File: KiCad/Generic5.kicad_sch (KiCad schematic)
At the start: 28 parts, among them J1 Conn_01x04, J2 USB-C, U1 ESP32-PICO-MINI-02, U2 FT231XQ, U3 LMR16006+FB

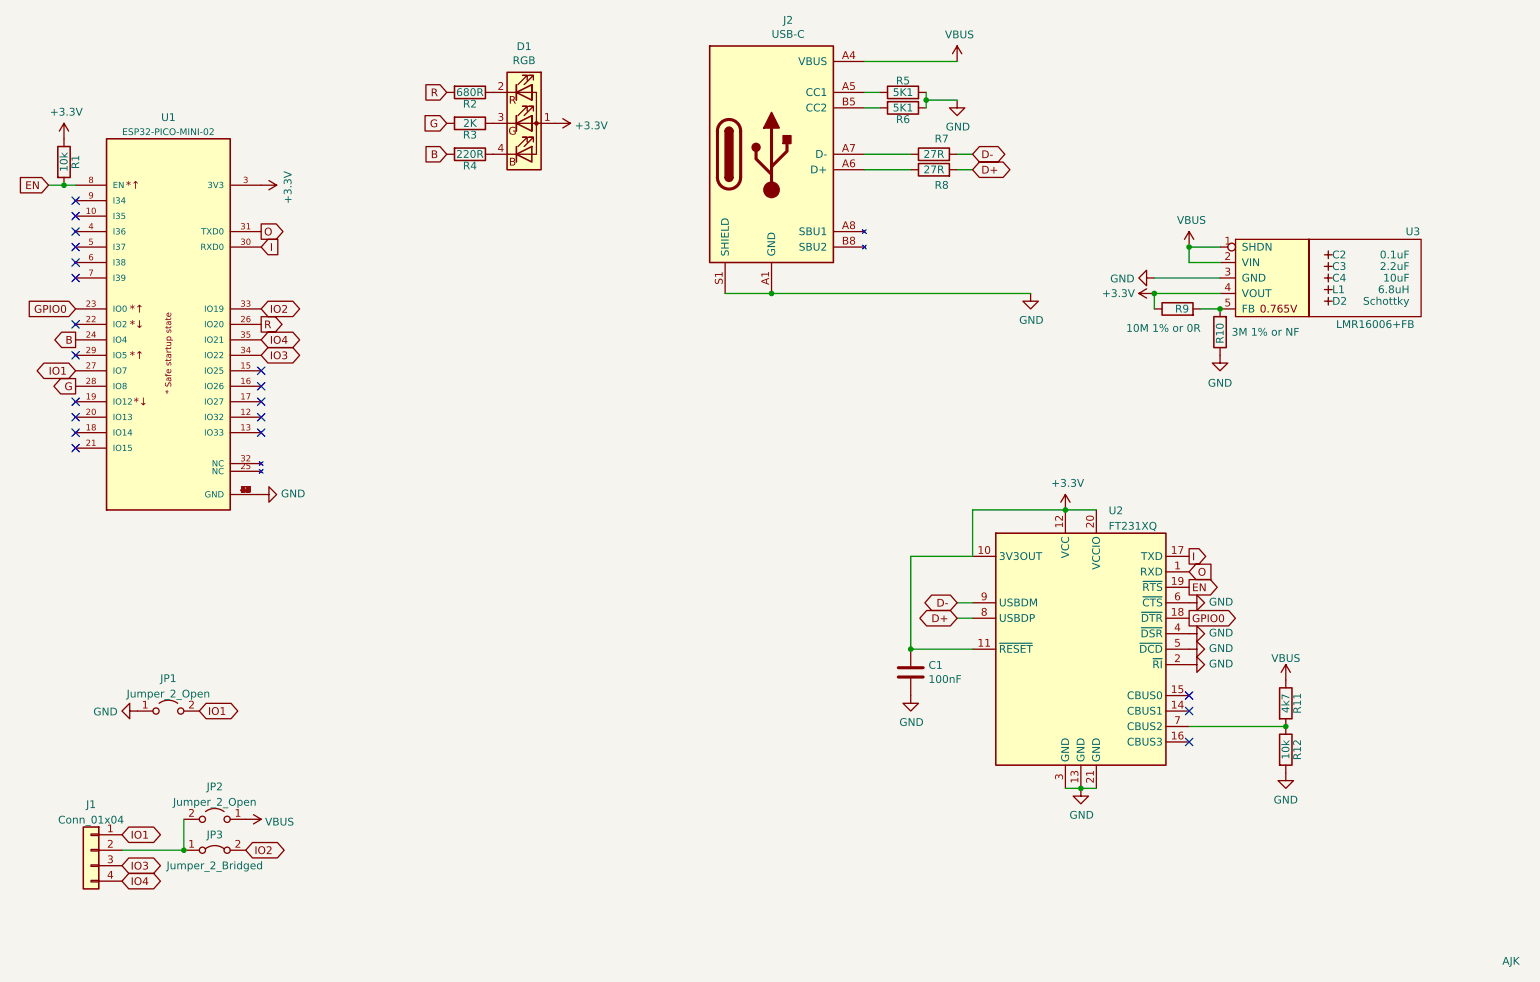
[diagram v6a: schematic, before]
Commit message: FET and diode logic
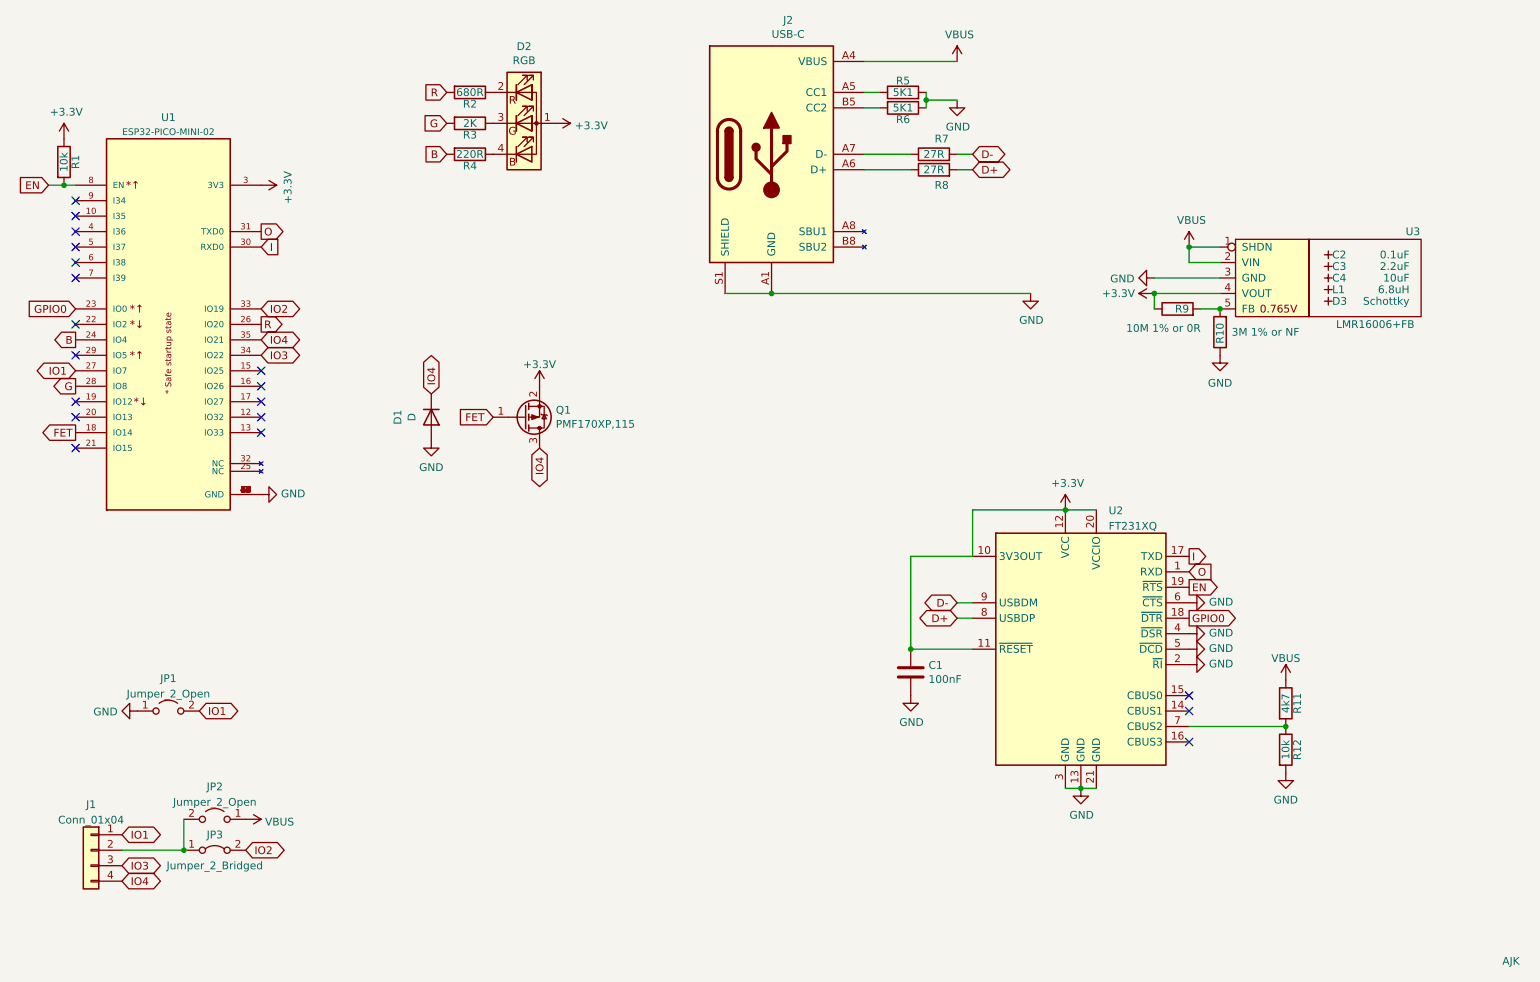
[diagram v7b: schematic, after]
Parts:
- added D1: D, Diode_SMD:D_1206_3216Metric, symbol Device:D
- added Q1: PMF170XP,115, Package_TO_SOT_SMD:SOT-323_SC-70, symbol Device:Q_PMOS_GSD
- renumbered D1 to D2, D2 to D3
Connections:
- net +3V3: now also Q1.2 (S)
- net GND: now also D1.2 (A)
- net IO4: now also D1.1 (K), Q1.3 (D)
- net FET: now reaches U1.18 (IO14)
- net FET: now also Q1.1 (G)
- no-connect marks 20 -> 19
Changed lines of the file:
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@@
   (no_connect (at 43.18 58.42))
   (no_connect (at 43.18 83.82))
-  (no_connect (at 43.18 86.36))
   (no_connect (at 73.66 83.82))
   (wire (pts (xy 226.06 134.62) (xy 241.935 134.62))
@@
     )
   )
+  (global_label "IO4" (shape bidirectional) (at 101.6 80.01 90) (fields_autoplaced)
+    (effects (font (size 1.27 1.27)) (justify left))
+    (property "Intersheet References" "${INTERSHEET_REFS}" (id 0) (at 16.51 160.655 0)
+      (effects (font (size 1.27 1.27)) hide)
+    )
+  )
   (global_label "IO2" (shape bidirectional) (at 71.12 154.94 0) (fields_autoplaced)
     (effects (font (size 1.27 1.27)) (justify left))
@@
     (property "Intersheet References" "${INTERSHEET_REFS}" (id 0) (at -6.985 -19.05 0)
       (effects (font (size 1.27 1.27)) hide)
+    )
+  )
+  (global_label "IO4" (shape bidirectional) (at 119.38 88.9 270) (fields_autoplaced)
+    (effects (font (size 1.27 1.27)) (justify right))
+    (property "Intersheet References" "${INTERSHEET_REFS}" (id 0) (at 204.47 8.255 0)
+      (effects (font (size 1.27 1.27)) hide)
+    )
+  )
+  (global_label "FET" (shape output) (at 43.18 86.36 180) (fields_autoplaced)
+    (effects (font (size 1.27 1.27)) (justify right))
+    (property "Intersheet References" "${INTERSHEET_REFS}" (id 0) (at 37.6506 86.2806 0)
+      (effects (font (size 1.27 1.27)) (justify right) hide)
     )
   )
@@
     )
   )
+  (global_label "FET" (shape input) (at 111.76 83.82 180) (fields_autoplaced)
+    (effects (font (size 1.27 1.27)) (justify right))
+    (property "Intersheet References" "${INTERSHEET_REFS}" (id 0) (at 106.2306 83.7406 0)
+      (effects (font (size 1.27 1.27)) (justify right) hide)
+    )
+  )
   (global_label "IO4" (shape bidirectional) (at 50.8 160.02 0) (fields_autoplaced)
     (effects (font (size 1.27 1.27)) (justify left))
@@
   (symbol (lib_id "Device:LED_ARGB") (at 116.84 35.56 0) (unit 1)
     (in_bom yes) (on_board yes)
-    (property "Reference" "D1" (id 0) (at 116.84 22.9362 0))
+    (property "Reference" "D2" (id 0) (at 116.84 22.9362 0))
     (property "Value" "RGB" (id 1) (at 116.84 25.2476 0))
     (property "Footprint" "RevK:LED-RGB-1.6x1.6" (id 2) (at 116.84 36.83 0)
@@
   (symbol (lib_id "RevK:Hidden") (at 248.92 64.77 0) (unit 1)
     (in_bom yes) (on_board yes)
-    (property "Reference" "D2" (id 0) (at 249.555 64.77 0)
+    (property "Reference" "D3" (id 0) (at 249.555 64.77 0)
       (effects (font (size 1.27 1.27)) (justify left))
     )
@@
     (pin "1")
   )
+  (symbol (lib_id "Device:Q_PMOS_GSD") (at 116.84 83.82 0) (mirror x) (unit 1)
+    (in_bom yes) (on_board yes)
+    (property "Reference" "Q1" (id 0) (at 122.047 82.6516 0)
+      (effects (font (size 1.27 1.27)) (justify left))
+    )
+    (property "Value" "PMF170XP,115" (id 1) (at 122.047 84.963 0)
+      (effects (font (size 1.27 1.27)) (justify left))
+    )
+    (property "Footprint" "Package_TO_SOT_SMD:SOT-323_SC-70" (id 2) (at 121.92 86.36 0)
+      (effects (font (size 1.27 1.27)) hide)
+    )
+    (property "Datasheet" "~" (id 3) (at 116.84 83.82 0)
+      (effects (font (size 1.27 1.27)) hide)
+    )
+    (property "Note" "Any P-Channel SOT323 that does 3.3V/0.5A" (id 4) (at 116.84 83.82 0)
+      (effects (font (size 1.27 1.27)) hide)
+    )
+    (pin "1")
+    (pin "2")
+    (pin "3")
+  )
   (symbol (lib_id "power:GND") (at 231.14 73.66 0) (unit 1)
     (in_bom yes) (on_board yes) (fields_autoplaced)
@@
     )
     (property "Datasheet" "" (id 3) (at 53.34 132.08 0)
+      (effects (font (size 1.27 1.27)) hide)
+    )
+    (pin "1")
+  )
+  (symbol (lib_id "power:+3.3V") (at 119.38 78.74 0) (unit 1)
+    (in_bom yes) (on_board yes) (fields_autoplaced)
+    (property "Reference" "#PWR0101" (id 0) (at 119.38 82.55 0)
+      (effects (font (size 1.27 1.27)) hide)
+    )
+    (property "Value" "+3.3V" (id 1) (at 119.38 75.1642 0))
+    (property "Footprint" "" (id 2) (at 119.38 78.74 0)
+      (effects (font (size 1.27 1.27)) hide)
+    )
+    (property "Datasheet" "" (id 3) (at 119.38 78.74 0)
       (effects (font (size 1.27 1.27)) hide)
     )
@@
     (pin "2")
   )
+  (symbol (lib_id "power:GND") (at 101.6 87.63 0) (unit 1)
+    (in_bom yes) (on_board yes) (fields_autoplaced)
+    (property "Reference" "#PWR?" (id 0) (at 101.6 93.98 0)
+      (effects (font (size 1.27 1.27)) hide)
+    )
+    (property "Value" "GND" (id 1) (at 101.6 92.0734 0))
+    (property "Footprint" "" (id 2) (at 101.6 87.63 0)
+      (effects (font (size 1.27 1.27)) hide)
+    )
+    (property "Datasheet" "" (id 3) (at 101.6 87.63 0)
+      (effects (font (size 1.27 1.27)) hide)
+    )
+    (pin "1")
+  )
   (symbol (lib_id "Connector_Generic:Conn_01x04") (at 45.72 154.94 0) (mirror y) (unit 1)
     (in_bom yes) (on_board yes) (fields_autoplaced)
@@
     (pin "5")
   )
+  (symbol (lib_id "Device:D") (at 101.6 83.82 270) (unit 1)
+    (in_bom yes) (on_board yes)
+    (property "Reference" "D1" (id 0) (at 96.0882 83.82 0))
+    (property "Value" "D" (id 1) (at 98.3996 83.82 0))
+    (property "Footprint" "Diode_SMD:D_1206_3216Metric" (id 2) (at 101.6 83.82 0)
+      (effects (font (size 1.27 1.27)) hide)
+    )
+    (property "Datasheet" "~" (id 3) (at 101.6 83.82 0)
+      (effects (font (size 1.27 1.27)) hide)
+    )
+    (pin "1")
+    (pin "2")
+  )
   (symbol (lib_id "Device:R") (at 224.155 66.04 90) (unit 1)
     (in_bom yes) (on_board yes)
@@
       (reference "#PWR022") (unit 1) (value "GND") (footprint "")
     )
+    (path "/5a99768e-d25b-4632-aa33-9050e210a6d2"
+      (reference "#PWR0101") (unit 1) (value "+3.3V") (footprint "")
+    )
+    (path "/851f4633-6493-46b9-aca3-fcb06a4992b7"
+      (reference "#PWR?") (unit 1) (value "GND") (footprint "")
+    )
     (path "/00000000-0000-0000-0000-0000609259a6"
       (reference "C1") (unit 1) (value "100nF") (footprint "RevK:C_0603")
@@
       (reference "C4") (unit 1) (value "10uF") (footprint "RevK:Hidden")
     )
+    (path "/eff204ef-5a36-42db-9320-eea32d40129b"
+      (reference "D1") (unit 1) (value "D") (footprint "Diode_SMD:D_1206_3216Metric")
+    )
     (path "/00000000-0000-0000-0000-000060cf36bc"
-      (reference "D1") (unit 1) (value "RGB") (footprint "RevK:LED-RGB-1.6x1.6")
+      (reference "D2") (unit 1) (value "RGB") (footprint "RevK:LED-RGB-1.6x1.6")
     )
     (path "/00000000-0000-0000-0000-0000610fe5d2"
-      (reference "D2") (unit 1) (value "Schottky") (footprint "RevK:Hidden")
+      (reference "D3") (unit 1) (value "Schottky") (footprint "RevK:Hidden")
     )
     (path "/9708f4f4-75f9-41be-ad42-df364d60ab1d"
@@
       (reference "Logo1") (unit 1) (value "AJK") (footprint "RevK:AJK")
     )
+    (path "/3f04a526-2075-4270-9368-cb856628e9fe"
+      (reference "Q1") (unit 1) (value "PMF170XP,115") (footprint "Package_TO_SOT_SMD:SOT-323_SC-70")
+    )
     (path "/3b6e2e43-685e-4e7b-97b9-8f290ca51417"

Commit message: Changed FET drive to pin 3 on Generic5, and reverted Generic3
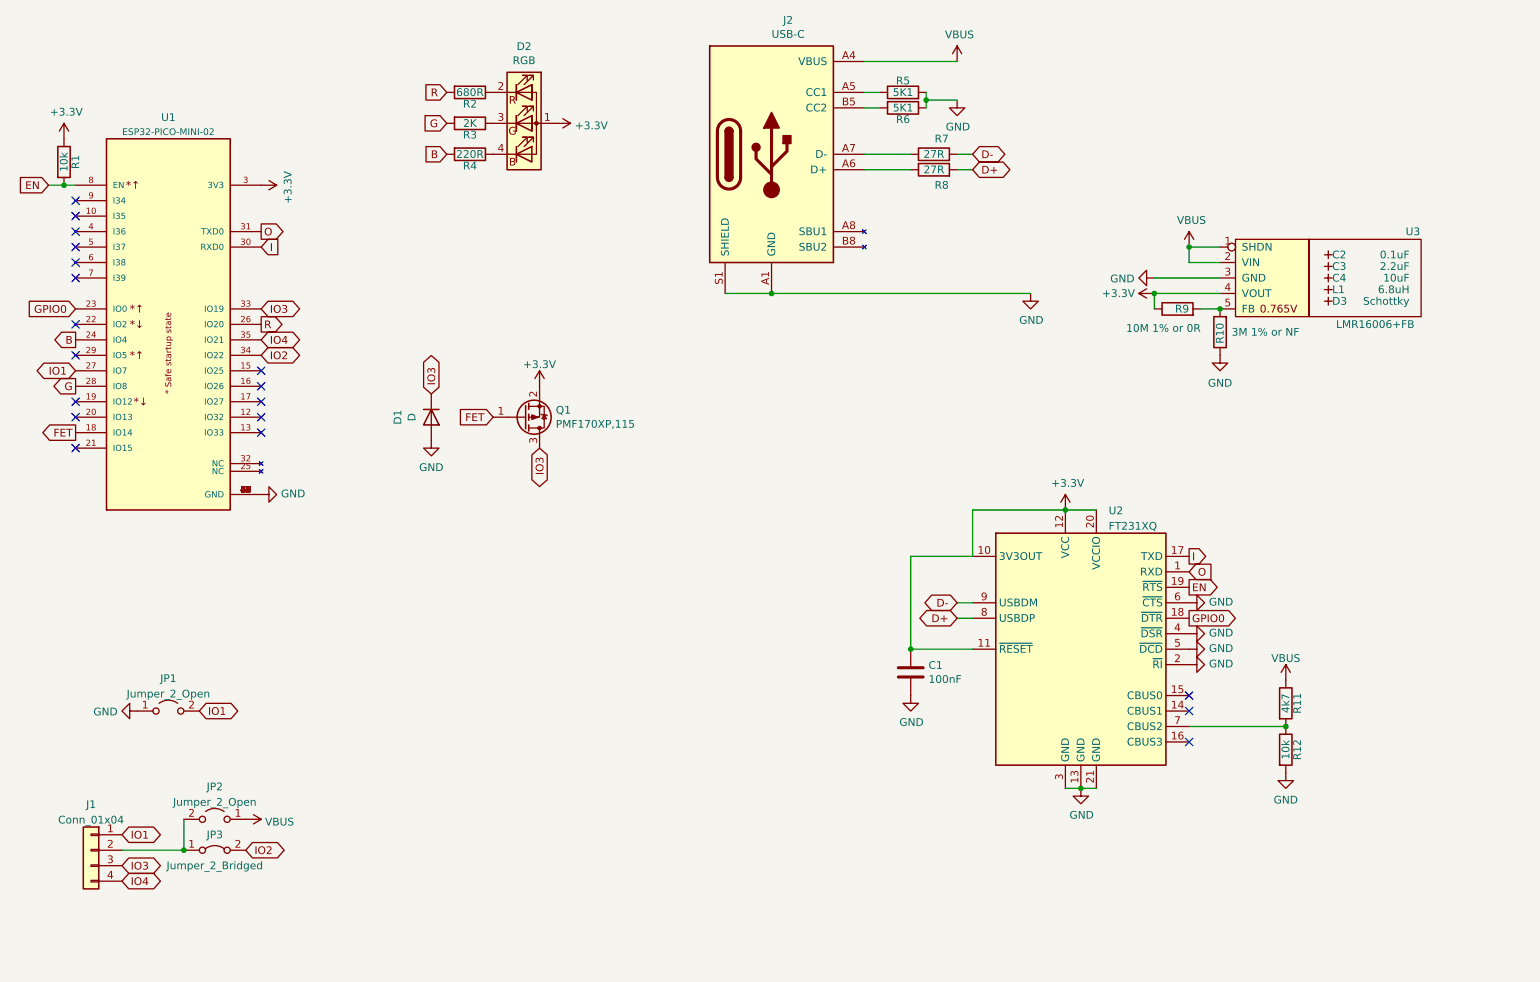
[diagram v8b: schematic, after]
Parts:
- removed Logo1: AJK, RevK:AJK, symbol RevK:AJK
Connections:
- net IO2: now also U1.34 (IO22); no longer U1.33 (IO19)
- net IO3: now also D1.1 (K), Q1.3 (D), U1.33 (IO19); no longer U1.34 (IO22)
- net IO4: no longer D1.1 (K), Q1.3 (D)
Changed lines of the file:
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@@
     )
   )
-  (global_label "IO3" (shape bidirectional) (at 73.66 73.66 0) (fields_autoplaced)
-    (effects (font (size 1.27 1.27)) (justify left))
-    (property "Intersheet References" "${INTERSHEET_REFS}" (id 0) (at -6.985 31.75 0)
+  (global_label "IO3" (shape bidirectional) (at 73.66 66.04 0) (fields_autoplaced)
+    (effects (font (size 1.27 1.27)) (justify left))
+    (property "Intersheet References" "${INTERSHEET_REFS}" (id 0) (at -6.985 24.13 0)
       (effects (font (size 1.27 1.27)) hide)
     )
@@
     )
   )
-  (global_label "IO2" (shape bidirectional) (at 73.66 66.04 0) (fields_autoplaced)
-    (effects (font (size 1.27 1.27)) (justify left))
-    (property "Intersheet References" "${INTERSHEET_REFS}" (id 0) (at -6.985 6.35 0)
+  (global_label "IO2" (shape bidirectional) (at 73.66 73.66 0) (fields_autoplaced)
+    (effects (font (size 1.27 1.27)) (justify left))
+    (property "Intersheet References" "${INTERSHEET_REFS}" (id 0) (at -6.985 13.97 0)
       (effects (font (size 1.27 1.27)) hide)
     )
@@
     )
   )
-  (global_label "IO4" (shape bidirectional) (at 101.6 80.01 90) (fields_autoplaced)
-    (effects (font (size 1.27 1.27)) (justify left))
-    (property "Intersheet References" "${INTERSHEET_REFS}" (id 0) (at 16.51 160.655 0)
-      (effects (font (size 1.27 1.27)) hide)
+  (global_label "IO3" (shape bidirectional) (at 101.6 80.01 90) (fields_autoplaced)
+    (effects (font (size 1.27 1.27)) (justify left))
+    (property "Intersheet References" "${INTERSHEET_REFS}" (id 0) (at 101.5206 74.541 90)
+      (effects (font (size 1.27 1.27)) (justify left) hide)
     )
   )
@@
     )
   )
-  (global_label "IO4" (shape bidirectional) (at 119.38 88.9 270) (fields_autoplaced)
+  (global_label "IO3" (shape bidirectional) (at 119.38 88.9 270) (fields_autoplaced)
     (effects (font (size 1.27 1.27)) (justify right))
-    (property "Intersheet References" "${INTERSHEET_REFS}" (id 0) (at 204.47 8.255 0)
-      (effects (font (size 1.27 1.27)) hide)
+    (property "Intersheet References" "${INTERSHEET_REFS}" (id 0) (at 119.3006 94.369 90)
+      (effects (font (size 1.27 1.27)) (justify right) hide)
     )
   )
@@
   (symbol (lib_id "power:GND") (at 101.6 87.63 0) (unit 1)
     (in_bom yes) (on_board yes) (fields_autoplaced)
-    (property "Reference" "#PWR?" (id 0) (at 101.6 93.98 0)
+    (property "Reference" "#PWR0102" (id 0) (at 101.6 93.98 0)
       (effects (font (size 1.27 1.27)) hide)
     )
@@
     (pin "4")
   )
-  (symbol (lib_id "RevK:AJK") (at 276.86 172.72 0) (unit 1)
-    (in_bom no) (on_board yes) (fields_autoplaced)
-    (property "Reference" "Logo1" (id 0) (at 276.86 170.18 0)
-      (effects (font (size 1.27 1.27)) hide)
-    )
-    (property "Value" "AJK" (id 1) (at 277.495 173.1538 0)
-      (effects (font (size 1.27 1.27)) (justify left))
-    )
-    (property "Footprint" "RevK:AJK" (id 2) (at 276.86 175.26 0)
-      (effects (font (size 1.27 1.27)) hide)
-    )
-    (property "Datasheet" "" (id 3) (at 276.86 175.26 0)
-      (effects (font (size 1.27 1.27)) hide)
-    )
-    (property "Note" "Non part, PCB printed" (id 4) (at 276.86 172.72 0)
-      (effects (font (size 1.27 1.27)) hide)
-    )
-  )
   (symbol (lib_id "Jumper:Jumper_2_Bridged") (at 66.04 154.94 0) (unit 1)
     (in_bom no) (on_board yes)
@@
     )
     (path "/851f4633-6493-46b9-aca3-fcb06a4992b7"
-      (reference "#PWR?") (unit 1) (value "GND") (footprint "")
+      (reference "#PWR0102") (unit 1) (value "GND") (footprint "")
     )
     (path "/00000000-0000-0000-0000-0000609259a6"
@@
       (reference "L1") (unit 1) (value "6.8uH") (footprint "RevK:Hidden")
     )
-    (path "/a38dd5c8-07fd-48c9-a981-784a5fc4f1d1"
-      (reference "Logo1") (unit 1) (value "AJK") (footprint "RevK:AJK")
-    )
     (path "/3f04a526-2075-4270-9368-cb856628e9fe"
